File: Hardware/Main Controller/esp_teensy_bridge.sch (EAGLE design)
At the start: 10 parts, among them IC1 BQ79600PWRQ1

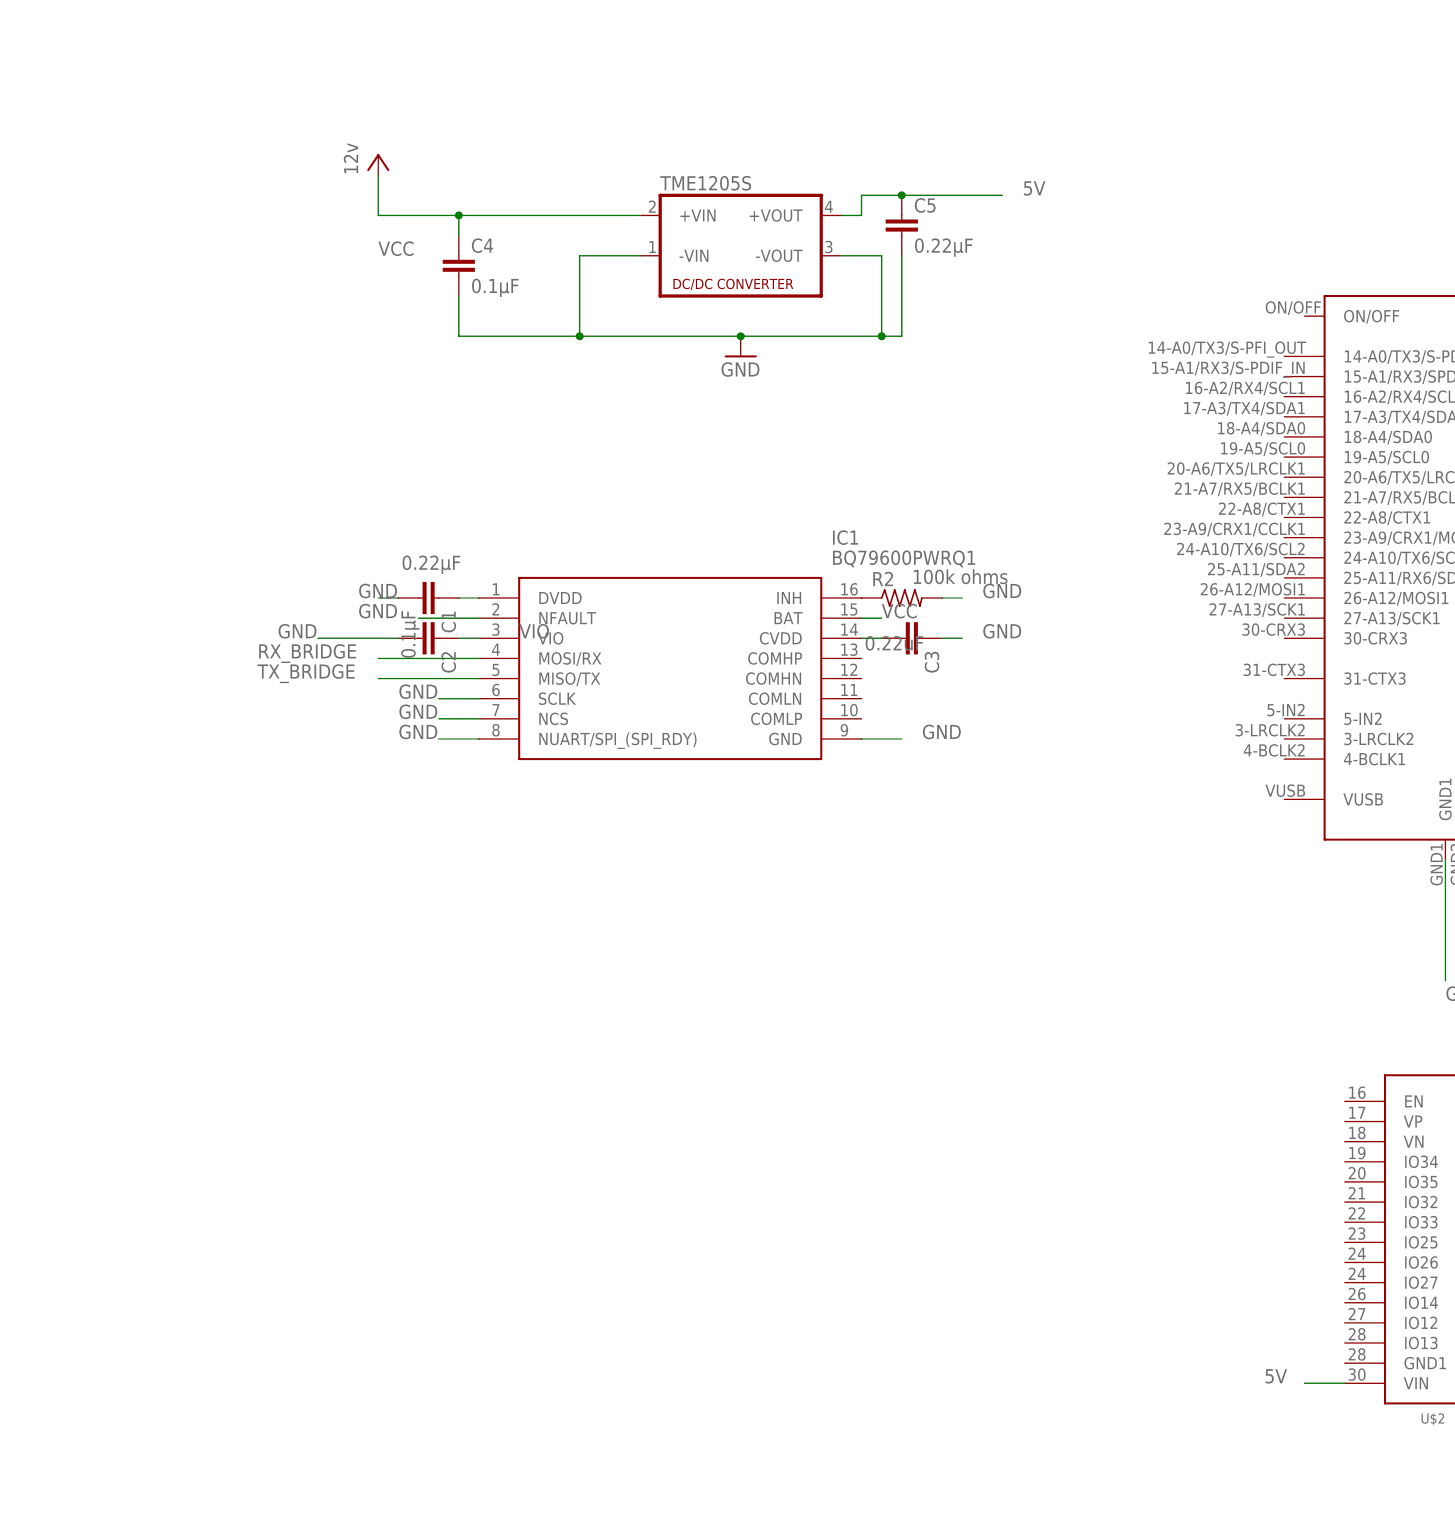
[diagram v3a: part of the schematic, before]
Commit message: Update esp_teensy_bridge.sch
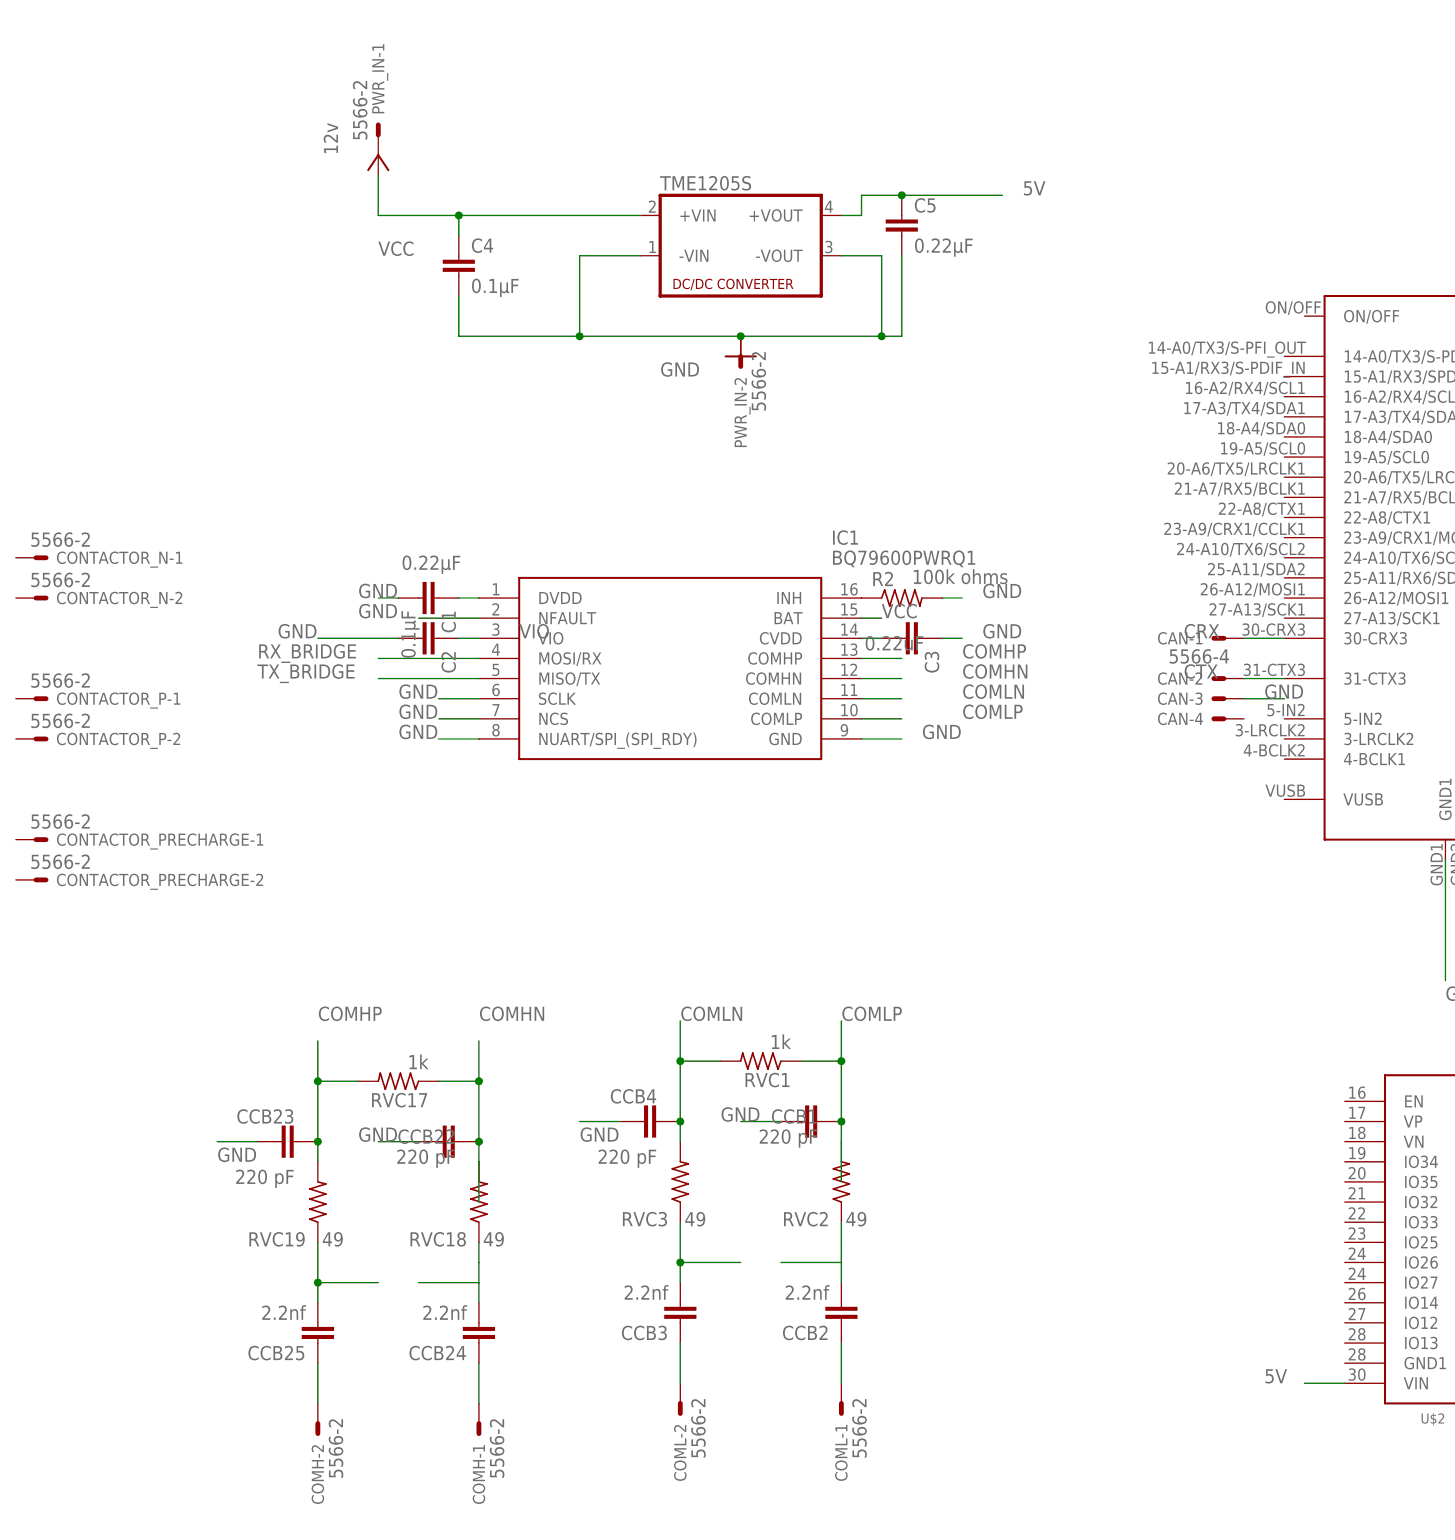
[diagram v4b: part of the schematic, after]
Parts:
- added CAN: 5566-4, con-molex:5566-4
- added CCB1, CCB22, CCB23, CCB4: 220 pF, capacitor-wima:C2.5/2
- added CCB2, CCB24, CCB25, CCB3: 2.2nf, capacitor-wima:C2.5/2
- added COMH, COML, CONTACTOR_N, CONTACTOR_P, CONTACTOR_PRECHARGE, PWR_IN: 5566-2, con-molex:5566-2
- added RVC1, RVC17: 1k, rcl:R-US_R0603
- added RVC18, RVC19, RVC2, RVC3: 49, rcl:R-US_R0603
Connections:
- new net COMHN: CCB22.2, IC1.COMHN, RVC17.1, RVC18.2
- new net COMHP: CCB23.2, IC1.COMHP, RVC17.2, RVC19.2
- new net COMLN: CCB4.2, IC1.COMLN, RVC1.2, RVC3.2
- new net COMLP: CCB1.2, IC1.COMLP, RVC1.1, RVC2.2
- new net CRX: CAN-1.S, U$1.30-CRX3
- new net CTX: CAN-2.S, U$1.31-CTX3
- new net N$6: CCB3.2, RVC3.1
- new net N$66: CCB25.1, COMH-2.S
- new net N$67: CCB25.2, RVC19.1
- new net N$68: CCB24.2, RVC18.1
- new net N$69: CCB24.1, COMH-1.S
- new net N$7: CCB2.2, RVC2.1
- new net N$8: CCB2.1, COML-1.S
- new net N$9: CCB3.1, COML-2.S
- net GND: now also CAN-3.S, CCB1.1, CCB22.1, CCB23.1, CCB4.1, PWR_IN-2.S

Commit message: finished main board
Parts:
- added Q1, Q2, Q3: SI7611DN-T1-GE3, SI7611DN-T1-GE3:SI7611DN-T1-GE3
- added R1, R3: 10k ohm, rcl:R-US_0204/2V
- added R4: 10km, rcl:R-US_0204/2V
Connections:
- new net CONTACTORN_CTRL: Q1.G, R1.2, U$1.32-OUT1B
- new net CONTACTORPRECHARGE_CTRL: Q3.G, R4.2, U$1.6-OUT1D
- new net CONTACTORP_CTRL: Q2.G, R3.2, U$1.9-OUT1C
- new net N$12: CONTACTOR_PRECHARGE-2.S, Q3.S
- new net N$2: CONTACTOR_P-2.S, Q2.S
- new net N$5: CONTACTOR_N-2.S, Q1.S
- net GND: now also Q1.D, Q2.D, Q3.D, R1.1, R3.1, R4.1
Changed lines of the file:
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@@
 <part name="CONTACTOR_P" library="con-molex" library_urn="urn:adsk.eagle:library:165" deviceset="5566-2" device="" package3d_urn="urn:adsk.eagle:package:8078583/1"/>
 <part name="CONTACTOR_PRECHARGE" library="con-molex" library_urn="urn:adsk.eagle:library:165" deviceset="5566-2" device="" package3d_urn="urn:adsk.eagle:package:8078583/1"/>
+<part name="Q1" library="SI7611DN-T1-GE3" deviceset="SI7611DN-T1-GE3" device=""/>
+<part name="Q2" library="SI7611DN-T1-GE3" deviceset="SI7611DN-T1-GE3" device=""/>
+<part name="Q3" library="SI7611DN-T1-GE3" deviceset="SI7611DN-T1-GE3" device=""/>
+<part name="R1" library="rcl" library_urn="urn:adsk.eagle:library:334" deviceset="R-US_" device="0204/2V" package3d_urn="urn:adsk.eagle:package:23495/1" value="10k ohm"/>
+<part name="R3" library="rcl" library_urn="urn:adsk.eagle:library:334" deviceset="R-US_" device="0204/2V" package3d_urn="urn:adsk.eagle:package:23495/1" value="10k ohm"/>
+<part name="R4" library="rcl" library_urn="urn:adsk.eagle:library:334" deviceset="R-US_" device="0204/2V" package3d_urn="urn:adsk.eagle:package:23495/1" value="10km"/>
 </parts>
 <sheets>
@@
 <attribute name="NAME" x="-116.84" y="29.718" size="1.524" layer="95"/>
 <attribute name="VALUE" x="-120.142" y="31.877" size="1.778" layer="96"/>
+</instance>
+<instance part="Q1" gate="G$1" x="-132.08" y="68.58" smashed="yes">
+<attribute name="VALUE" x="-140.97796875" y="62.224309375" size="1.779590625" layer="96"/>
+<attribute name="NAME" x="-140.987490625" y="72.397490625" size="1.7815" layer="95"/>
+</instance>
+<instance part="Q2" gate="G$1" x="-132.08" y="50.8" smashed="yes">
+<attribute name="VALUE" x="-140.97796875" y="44.444309375" size="1.779590625" layer="96"/>
+<attribute name="NAME" x="-140.987490625" y="54.617490625" size="1.7815" layer="95"/>
+</instance>
+<instance part="Q3" gate="G$1" x="-132.08" y="33.02" smashed="yes">
+<attribute name="VALUE" x="-140.97796875" y="26.664309375" size="1.779590625" layer="96"/>
+<attribute name="NAME" x="-140.987490625" y="36.837490625" size="1.7815" layer="95"/>
+</instance>
+<instance part="R1" gate="G$1" x="-139.7" y="76.2" smashed="yes">
+<attribute name="NAME" x="-143.51" y="77.6986" size="1.778" layer="95"/>
+<attribute name="VALUE" x="-143.51" y="72.898" size="1.778" layer="96"/>
+</instance>
+<instance part="R3" gate="G$1" x="-139.7" y="58.42" smashed="yes">
+<attribute name="NAME" x="-143.51" y="59.9186" size="1.778" layer="95"/>
+<attribute name="VALUE" x="-143.51" y="55.118" size="1.778" layer="96"/>
+</instance>
+<instance part="R4" gate="G$1" x="-139.7" y="40.64" smashed="yes">
+<attribute name="NAME" x="-143.51" y="42.1386" size="1.778" layer="95"/>
+<attribute name="VALUE" x="-143.51" y="37.338" size="1.778" layer="96"/>
 </instance>
 </instances>
@@
 <label x="35.56" y="53.34" size="1.778" layer="95"/>
 </segment>
+<segment>
+<pinref part="Q1" gate="G$1" pin="D"/>
+<wire x1="-129.54" y1="63.5" x2="-129.54" y2="60.96" width="0.1524" layer="91"/>
+<label x="-129.54" y="58.42" size="1.778" layer="95"/>
+<wire x1="-129.54" y1="60.96" x2="-144.78" y2="60.96" width="0.1524" layer="91"/>
+<pinref part="R1" gate="G$1" pin="1"/>
+<wire x1="-144.78" y1="76.2" x2="-144.78" y2="60.96" width="0.1524" layer="91"/>
+</segment>
+<segment>
+<pinref part="Q2" gate="G$1" pin="D"/>
+<wire x1="-129.54" y1="45.72" x2="-129.54" y2="43.18" width="0.1524" layer="91"/>
+<label x="-129.54" y="43.18" size="1.778" layer="95"/>
+<pinref part="R3" gate="G$1" pin="1"/>
+<wire x1="-144.78" y1="58.42" x2="-144.78" y2="43.18" width="0.1524" layer="91"/>
+<wire x1="-144.78" y1="43.18" x2="-129.54" y2="43.18" width="0.1524" layer="91"/>
+</segment>
+<segment>
+<pinref part="Q3" gate="G$1" pin="D"/>
+<wire x1="-129.54" y1="27.94" x2="-129.54" y2="25.4" width="0.1524" layer="91"/>
+<label x="-129.54" y="22.86" size="1.778" layer="95"/>
+<pinref part="R4" gate="G$1" pin="1"/>
+<wire x1="-144.78" y1="40.64" x2="-144.78" y2="25.4" width="0.1524" layer="91"/>
+<wire x1="-144.78" y1="25.4" x2="-129.54" y2="25.4" width="0.1524" layer="91"/>
+</segment>
 </net>
 <net name="NCS/CS" class="0">
@@
 </segment>
 </net>
+<net name="CONTACTORN_CTRL" class="0">
+<segment>
+<pinref part="Q1" gate="G$1" pin="G"/>
+<wire x1="-134.62" y1="71.12" x2="-134.62" y2="76.2" width="0.1524" layer="91"/>
+<label x="-137.16" y="76.2" size="1.778" layer="95"/>
+<pinref part="R1" gate="G$1" pin="2"/>
+</segment>
+<segment>
+<pinref part="U$1" gate="G$1" pin="32-OUT1B"/>
+<wire x1="93.98" y1="58.42" x2="99.06" y2="58.42" width="0.1524" layer="91"/>
+<label x="109.22" y="58.42" size="1.778" layer="95"/>
+</segment>
+</net>
+<net name="N$5" class="0">
+<segment>
+<pinref part="Q1" gate="G$1" pin="S"/>
+<wire x1="-129.54" y1="73.66" x2="-127" y2="73.66" width="0.1524" layer="91"/>
+<wire x1="-127" y1="73.66" x2="-127" y2="66.04" width="0.1524" layer="91"/>
+<pinref part="CONTACTOR_N" gate="-2" pin="S"/>
+<wire x1="-127" y1="66.04" x2="-121.92" y2="66.04" width="0.1524" layer="91"/>
+</segment>
+</net>
+<net name="N$2" class="0">
+<segment>
+<pinref part="Q2" gate="G$1" pin="S"/>
+<wire x1="-129.54" y1="55.88" x2="-127" y2="55.88" width="0.1524" layer="91"/>
+<pinref part="CONTACTOR_P" gate="-2" pin="S"/>
+<wire x1="-127" y1="55.88" x2="-127" y2="48.26" width="0.1524" layer="91"/>
+<wire x1="-127" y1="48.26" x2="-121.92" y2="48.26" width="0.1524" layer="91"/>
+</segment>
+</net>
+<net name="CONTACTORP_CTRL" class="0">
+<segment>
+<pinref part="Q2" gate="G$1" pin="G"/>
+<wire x1="-134.62" y1="53.34" x2="-134.62" y2="58.42" width="0.1524" layer="91"/>
+<pinref part="R3" gate="G$1" pin="2"/>
+<label x="-127" y="55.88" size="1.778" layer="95"/>
+</segment>
+<segment>
+<pinref part="U$1" gate="G$1" pin="9-OUT1C"/>
+<wire x1="93.98" y1="55.88" x2="99.06" y2="55.88" width="0.1524" layer="91"/>
+<label x="109.22" y="55.88" size="1.778" layer="95"/>
+</segment>
+</net>
+<net name="CONTACTORPRECHARGE_CTRL" class="0">
+<segment>
+<pinref part="R4" gate="G$1" pin="2"/>
+<pinref part="Q3" gate="G$1" pin="G"/>
+<wire x1="-134.62" y1="40.64" x2="-134.62" y2="35.56" width="0.1524" layer="91"/>
+<label x="-132.08" y="40.64" size="1.778" layer="95"/>
+</segment>
+<segment>
+<pinref part="U$1" gate="G$1" pin="6-OUT1D"/>
+<wire x1="93.98" y1="53.34" x2="99.06" y2="53.34" width="0.1524" layer="91"/>
+<label x="109.22" y="53.34" size="1.778" layer="95"/>
+</segment>
+</net>
+<net name="N$12" class="0">
+<segment>
+<pinref part="Q3" gate="G$1" pin="S"/>
+<wire x1="-129.54" y1="38.1" x2="-127" y2="38.1" width="0.1524" layer="91"/>
+<wire x1="-127" y1="38.1" x2="-127" y2="30.48" width="0.1524" layer="91"/>
+<pinref part="CONTACTOR_PRECHARGE" gate="-2" pin="S"/>
+<wire x1="-127" y1="30.48" x2="-121.92" y2="30.48" width="0.1524" layer="91"/>
+</segment>
+</net>

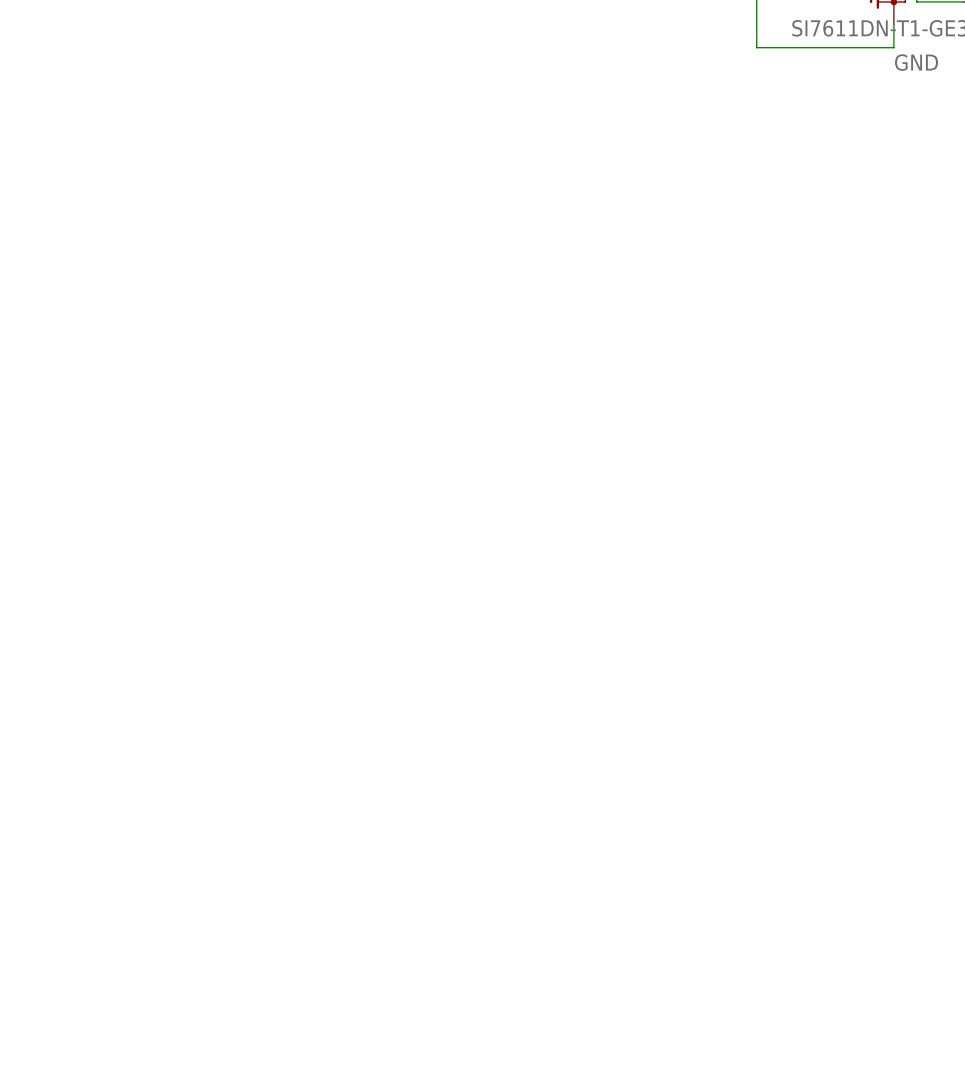
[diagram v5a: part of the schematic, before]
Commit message: Added com isolation to main board
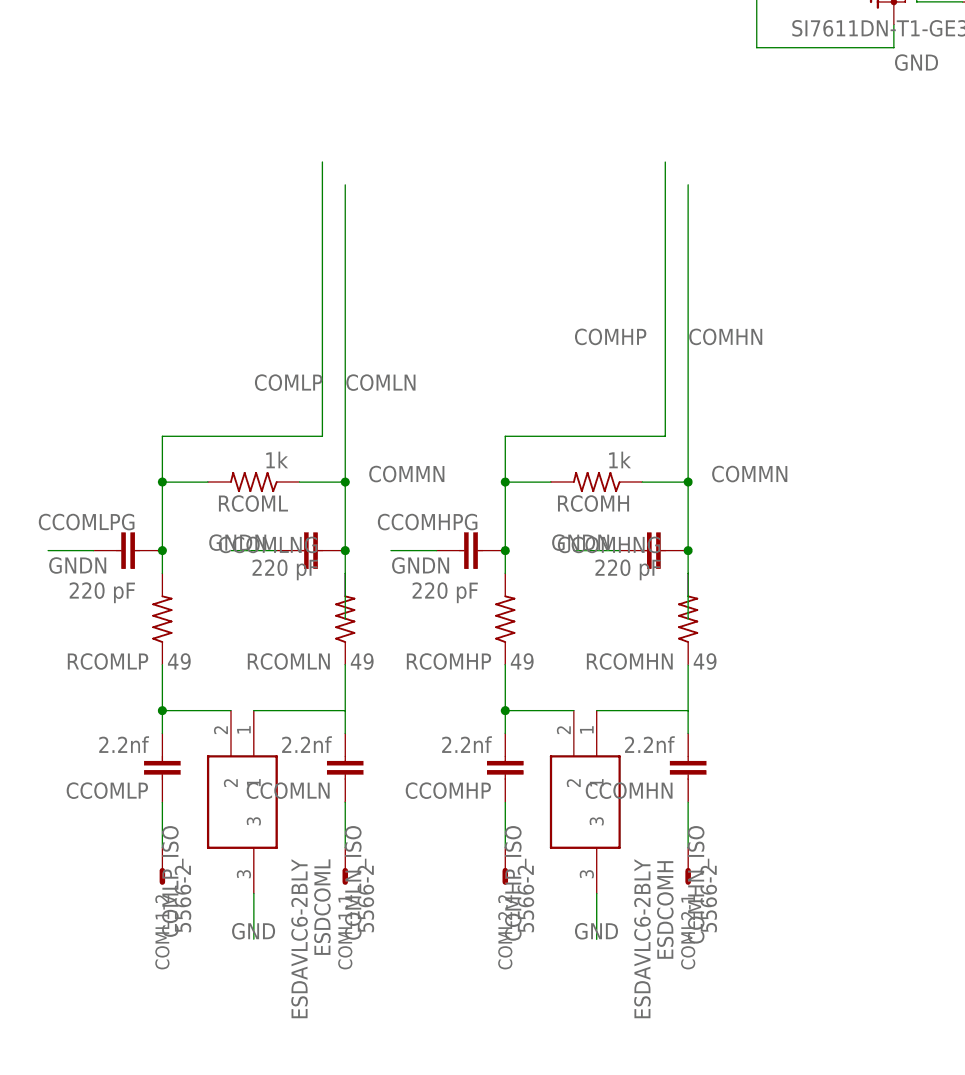
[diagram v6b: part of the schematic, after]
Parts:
- added CCOMHN, CCOMHP, CCOMLN, CCOMLP: 2.2nf, rcl:C-EUC0603
- added CCOMHNG, CCOMHPG, CCOMLNG, CCOMLPG: 220 pF, rcl:C-EUC0603
- added COML1, COML2: 5566-2, con-molex:5566-2
- added ESDCOMH, ESDCOML: ESDAVLC6-2BLY, ESDAVLC6-2BLY:ESDAVLC6-2BLY
- added RCOMH, RCOML: 1k, rcl:R-US_R0603
- added RCOMHN, RCOMHP, RCOMLN, RCOMLP: 49, rcl:R-US_R0603
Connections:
- new net COMHN_ISO: CCOMHN.1, COML2-1.S
- new net COMHP_ISO: CCOMHP.1, COML2-2.S
- new net COMLN_ISO: CCOMLN.1, COML1-1.S
- new net COMLP_ISO: CCOMLP.1, COML1-2.S
- new net GNDN: CCOMHNG.1, CCOMHPG.1, CCOMLNG.1, CCOMLPG.1
- new net N$10: CCOMLP.2, ESDCOML.2, RCOMLP.1
- new net N$11: CCOMLN.2, ESDCOML.1, RCOMLN.1
- new net N$15: CCOMHP.2, ESDCOMH.2, RCOMHP.1
- new net N$16: CCOMHN.2, ESDCOMH.1, RCOMHN.1
- net COMHN: now also CCOMHNG.2, RCOMH.1, RCOMHN.2
- net COMHP: now also CCOMHPG.2, RCOMH.2, RCOMHP.2
- net COMLN: now also CCOMLNG.2, RCOML.1, RCOMLN.2
- net COMLP: now also CCOMLPG.2, RCOML.2, RCOMLP.2
- net GND: now also ESDCOMH.3, ESDCOML.3
